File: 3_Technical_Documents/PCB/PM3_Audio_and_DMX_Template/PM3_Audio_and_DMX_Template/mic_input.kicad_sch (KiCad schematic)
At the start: 14 parts, among them U4 OPA322

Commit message: new push
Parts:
- renumbered C6 to C14, C7 to C15, C8 to C16, C9 to C17, C10 to C18, R11 to R15, R12 to R16, R13 to R17, R14 to R18, R15 to R19, R16 to R20, TP14 to TP10, U4 to U6
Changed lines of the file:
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@@
 		(dnp no)
 		(fields_autoplaced yes)
-		(property "Reference" "C8"
+		(property "Reference" "C16"
 			(at 99.06 39.37 90)
 			(effects
@@
 			(project ""
 				(path "/1f276d59-ad9b-4e70-a842-f3b7e562eb9b/2329d9ea-d5d7-4913-84c5-e85a54af032e/0553e14e-9a48-4ba5-90f9-f0331f773f30"
-					(reference "C8")
+					(reference "C16")
 					(unit 1)
 				)
@@
 		(dnp no)
 		(fields_autoplaced yes)
-		(property "Reference" "#PWR034"
+		(property "Reference" "#PWR048"
 			(at 53.34 115.57 0)
 			(effects
@@
 			(project ""
 				(path "/1f276d59-ad9b-4e70-a842-f3b7e562eb9b/2329d9ea-d5d7-4913-84c5-e85a54af032e/0553e14e-9a48-4ba5-90f9-f0331f773f30"
-					(reference "#PWR034")
+					(reference "#PWR048")
 					(unit 1)
 				)
@@
 		(dnp no)
 		(fields_autoplaced yes)
-		(property "Reference" "#PWR040"
+		(property "Reference" "#PWR054"
 			(at 153.67 111.76 0)
 			(effects
@@
 			(project ""
 				(path "/1f276d59-ad9b-4e70-a842-f3b7e562eb9b/2329d9ea-d5d7-4913-84c5-e85a54af032e/0553e14e-9a48-4ba5-90f9-f0331f773f30"
-					(reference "#PWR040")
+					(reference "#PWR054")
 					(unit 1)
 				)
@@
 		(dnp no)
 		(fields_autoplaced yes)
-		(property "Reference" "C7"
+		(property "Reference" "C15"
 			(at 78.359 77.47 90)
 			(effects
@@
 			(project ""
 				(path "/1f276d59-ad9b-4e70-a842-f3b7e562eb9b/2329d9ea-d5d7-4913-84c5-e85a54af032e/0553e14e-9a48-4ba5-90f9-f0331f773f30"
-					(reference "C7")
+					(reference "C15")
 					(unit 1)
 				)
@@
 		(dnp no)
 		(fields_autoplaced yes)
-		(property "Reference" "R13"
+		(property "Reference" "R17"
 			(at 86.36 113.0299 0)
 			(effects
@@
 			(project ""
 				(path "/1f276d59-ad9b-4e70-a842-f3b7e562eb9b/2329d9ea-d5d7-4913-84c5-e85a54af032e/0553e14e-9a48-4ba5-90f9-f0331f773f30"
-					(reference "R13")
+					(reference "R17")
 					(unit 1)
 				)
@@
 		(dnp no)
 		(fields_autoplaced yes)
-		(property "Reference" "R12"
+		(property "Reference" "R16"
 			(at 86.36 100.3299 0)
 			(effects
@@
 			(project ""
 				(path "/1f276d59-ad9b-4e70-a842-f3b7e562eb9b/2329d9ea-d5d7-4913-84c5-e85a54af032e/0553e14e-9a48-4ba5-90f9-f0331f773f30"
-					(reference "R12")
+					(reference "R16")
 					(unit 1)
 				)
@@
 		(dnp no)
 		(fields_autoplaced yes)
-		(property "Reference" "#PWR037"
+		(property "Reference" "#PWR051"
 			(at 99.06 128.27 0)
 			(effects
@@
 			(project "PM3_Audio_and_DMX"
 				(path "/1f276d59-ad9b-4e70-a842-f3b7e562eb9b/2329d9ea-d5d7-4913-84c5-e85a54af032e/0553e14e-9a48-4ba5-90f9-f0331f773f30"
-					(reference "#PWR037")
+					(reference "#PWR051")
 					(unit 1)
 				)
@@
 		(dnp no)
 		(fields_autoplaced yes)
-		(property "Reference" "C9"
+		(property "Reference" "C17"
 			(at 102.87 113.0299 0)
 			(effects
@@
 			(project "PM3_Audio_and_DMX"
 				(path "/1f276d59-ad9b-4e70-a842-f3b7e562eb9b/2329d9ea-d5d7-4913-84c5-e85a54af032e/0553e14e-9a48-4ba5-90f9-f0331f773f30"
-					(reference "C9")
+					(reference "C17")
 					(unit 1)
 				)
@@
 		(dnp no)
 		(fields_autoplaced yes)
-		(property "Reference" "R14"
+		(property "Reference" "R18"
 			(at 99.06 55.88 90)
 			(effects
@@
 			(project ""
 				(path "/1f276d59-ad9b-4e70-a842-f3b7e562eb9b/2329d9ea-d5d7-4913-84c5-e85a54af032e/0553e14e-9a48-4ba5-90f9-f0331f773f30"
-					(reference "R14")
+					(reference "R18")
 					(unit 1)
 				)
@@
 		(dnp no)
 		(fields_autoplaced yes)
-		(property "Reference" "R16"
+		(property "Reference" "R20"
 			(at 156.21 95.2499 0)
 			(effects
@@
 			(project ""
 				(path "/1f276d59-ad9b-4e70-a842-f3b7e562eb9b/2329d9ea-d5d7-4913-84c5-e85a54af032e/0553e14e-9a48-4ba5-90f9-f0331f773f30"
-					(reference "R16")
+					(reference "R20")
 					(unit 1)
 				)
@@
 		(dnp no)
 		(fields_autoplaced yes)
-		(property "Reference" "C6"
+		(property "Reference" "C14"
 			(at 76.2 113.0299 0)
 			(effects
@@
 			(project ""
 				(path "/1f276d59-ad9b-4e70-a842-f3b7e562eb9b/2329d9ea-d5d7-4913-84c5-e85a54af032e/0553e14e-9a48-4ba5-90f9-f0331f773f30"
-					(reference "C6")
+					(reference "C14")
 					(unit 1)
 				)
@@
 		(dnp no)
 		(fields_autoplaced yes)
-		(property "Reference" "#PWR033"
+		(property "Reference" "#PWR047"
 			(at 53.34 64.77 0)
 			(effects
@@
 			(project ""
 				(path "/1f276d59-ad9b-4e70-a842-f3b7e562eb9b/2329d9ea-d5d7-4913-84c5-e85a54af032e/0553e14e-9a48-4ba5-90f9-f0331f773f30"
-					(reference "#PWR033")
+					(reference "#PWR047")
 					(unit 1)
 				)
@@
 		(dnp no)
 		(fields_autoplaced yes)
-		(property "Reference" "R11"
+		(property "Reference" "R15"
 			(at 55.88 72.3899 0)
 			(effects
@@
 			(project ""
 				(path "/1f276d59-ad9b-4e70-a842-f3b7e562eb9b/2329d9ea-d5d7-4913-84c5-e85a54af032e/0553e14e-9a48-4ba5-90f9-f0331f773f30"
-					(reference "R11")
+					(reference "R15")
 					(unit 1)
 				)
@@
 		(dnp no)
 		(fields_autoplaced yes)
-		(property "Reference" "R15"
+		(property "Reference" "R19"
 			(at 128.27 81.28 90)
 			(effects
@@
 			(project ""
 				(path "/1f276d59-ad9b-4e70-a842-f3b7e562eb9b/2329d9ea-d5d7-4913-84c5-e85a54af032e/0553e14e-9a48-4ba5-90f9-f0331f773f30"
-					(reference "R15")
+					(reference "R19")
 					(unit 1)
 				)
@@
 		(on_board yes)
 		(dnp no)
-		(property "Reference" "U4"
+		(property "Reference" "U6"
 			(at 103.632 92.964 0)
 			(effects
@@
 			(project ""
 				(path "/1f276d59-ad9b-4e70-a842-f3b7e562eb9b/2329d9ea-d5d7-4913-84c5-e85a54af032e/0553e14e-9a48-4ba5-90f9-f0331f773f30"
-					(reference "U4")
+					(reference "U6")
 					(unit 1)
 				)
@@
 		(dnp no)
 		(fields_autoplaced yes)
-		(property "Reference" "#PWR038"
+		(property "Reference" "#PWR052"
 			(at 105.41 106.68 0)
 			(effects
@@
 			(project ""
 				(path "/1f276d59-ad9b-4e70-a842-f3b7e562eb9b/2329d9ea-d5d7-4913-84c5-e85a54af032e/0553e14e-9a48-4ba5-90f9-f0331f773f30"
-					(reference "#PWR038")
+					(reference "#PWR052")
 					(unit 1)
 				)
@@
 		(dnp no)
 		(fields_autoplaced yes)
-		(property "Reference" "#PWR039"
+		(property "Reference" "#PWR053"
 			(at 113.03 81.28 0)
 			(effects
@@
 			(project ""
 				(path "/1f276d59-ad9b-4e70-a842-f3b7e562eb9b/2329d9ea-d5d7-4913-84c5-e85a54af032e/0553e14e-9a48-4ba5-90f9-f0331f773f30"
-					(reference "#PWR039")
+					(reference "#PWR053")
 					(unit 1)
 				)
@@
 		(dnp no)
 		(fields_autoplaced yes)
-		(property "Reference" "#PWR035"
+		(property "Reference" "#PWR049"
 			(at 83.82 97.79 0)
 			(effects
@@
 			(project ""
 				(path "/1f276d59-ad9b-4e70-a842-f3b7e562eb9b/2329d9ea-d5d7-4913-84c5-e85a54af032e/0553e14e-9a48-4ba5-90f9-f0331f773f30"
-					(reference "#PWR035")
+					(reference "#PWR049")
 					(unit 1)
 				)
@@
 		(dnp no)
 		(fields_autoplaced yes)
-		(property "Reference" "TP14"
+		(property "Reference" "TP10"
 			(at 41.91 76.7079 0)
 			(effects
@@
 			(project "PM3_Audio_and_DMX"
 				(path "/1f276d59-ad9b-4e70-a842-f3b7e562eb9b/2329d9ea-d5d7-4913-84c5-e85a54af032e/0553e14e-9a48-4ba5-90f9-f0331f773f30"
-					(reference "TP14")
+					(reference "TP10")
 					(unit 1)
 				)
@@
 		(dnp no)
 		(fields_autoplaced yes)
-		(property "Reference" "C10"
+		(property "Reference" "C18"
 			(at 141.351 80.01 90)
 			(effects
@@
 			(project ""
 				(path "/1f276d59-ad9b-4e70-a842-f3b7e562eb9b/2329d9ea-d5d7-4913-84c5-e85a54af032e/0553e14e-9a48-4ba5-90f9-f0331f773f30"
-					(reference "C10")
+					(reference "C18")
 					(unit 1)
 				)
@@
 		(dnp no)
 		(fields_autoplaced yes)
-		(property "Reference" "#PWR036"
+		(property "Reference" "#PWR050"
 			(at 83.82 129.54 0)
 			(effects
@@
 			(project ""
 				(path "/1f276d59-ad9b-4e70-a842-f3b7e562eb9b/2329d9ea-d5d7-4913-84c5-e85a54af032e/0553e14e-9a48-4ba5-90f9-f0331f773f30"
-					(reference "#PWR036")
-					(unit 1)
-				)
+					(reference "#PWR050")
+					(unit 1)
+				)

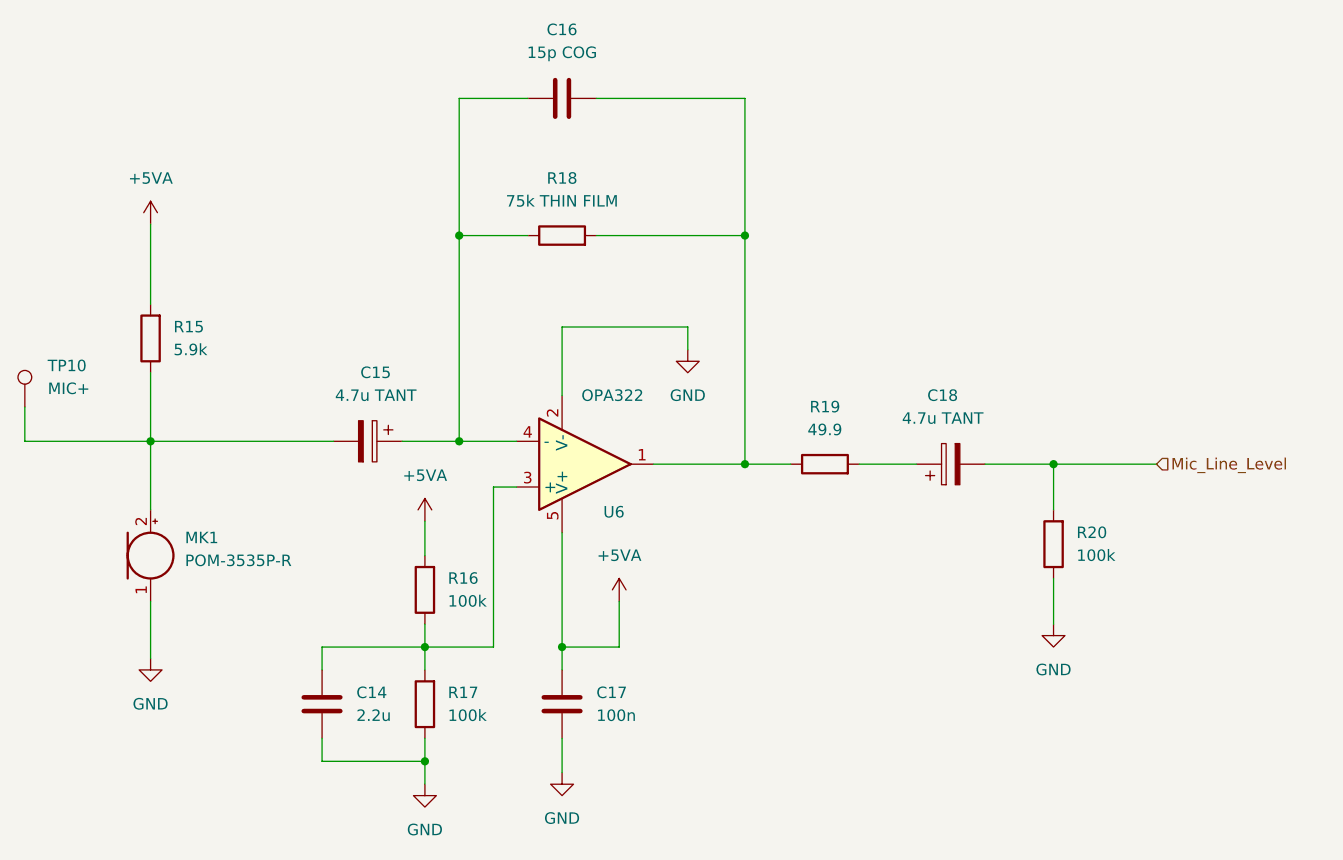
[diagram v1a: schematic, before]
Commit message: rework esp32, codec and layout
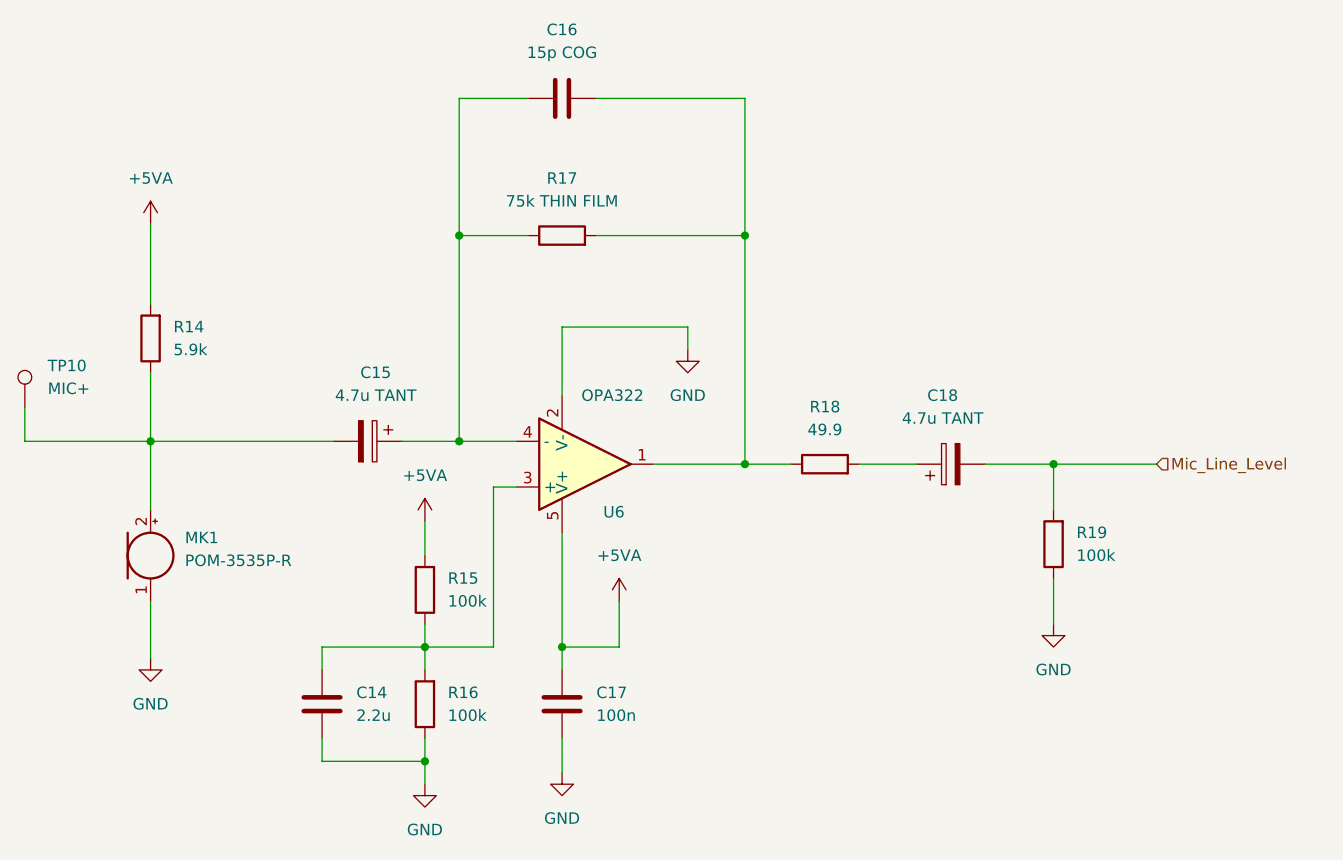
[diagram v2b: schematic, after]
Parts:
- renumbered R15 to R14, R16 to R15, R17 to R16, R18 to R17, R19 to R18, R20 to R19
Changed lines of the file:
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@@
 		(dnp no)
 		(fields_autoplaced yes)
-		(property "Reference" "#PWR048"
+		(property "Reference" "#PWR047"
 			(at 53.34 115.57 0)
 			(effects
@@
 			(project ""
 				(path "/1f276d59-ad9b-4e70-a842-f3b7e562eb9b/2329d9ea-d5d7-4913-84c5-e85a54af032e/0553e14e-9a48-4ba5-90f9-f0331f773f30"
-					(reference "#PWR048")
+					(reference "#PWR047")
 					(unit 1)
 				)
@@
 		(dnp no)
 		(fields_autoplaced yes)
-		(property "Reference" "#PWR054"
+		(property "Reference" "#PWR053"
 			(at 153.67 111.76 0)
 			(effects
@@
 			(project ""
 				(path "/1f276d59-ad9b-4e70-a842-f3b7e562eb9b/2329d9ea-d5d7-4913-84c5-e85a54af032e/0553e14e-9a48-4ba5-90f9-f0331f773f30"
-					(reference "#PWR054")
+					(reference "#PWR053")
 					(unit 1)
 				)
@@
 		(dnp no)
 		(fields_autoplaced yes)
-		(property "Reference" "R17"
+		(property "Reference" "R16"
 			(at 86.36 113.0299 0)
 			(effects
@@
 			(project ""
 				(path "/1f276d59-ad9b-4e70-a842-f3b7e562eb9b/2329d9ea-d5d7-4913-84c5-e85a54af032e/0553e14e-9a48-4ba5-90f9-f0331f773f30"
-					(reference "R17")
+					(reference "R16")
 					(unit 1)
 				)
@@
 		(dnp no)
 		(fields_autoplaced yes)
-		(property "Reference" "R16"
+		(property "Reference" "R15"
 			(at 86.36 100.3299 0)
 			(effects
@@
 			(project ""
 				(path "/1f276d59-ad9b-4e70-a842-f3b7e562eb9b/2329d9ea-d5d7-4913-84c5-e85a54af032e/0553e14e-9a48-4ba5-90f9-f0331f773f30"
-					(reference "R16")
+					(reference "R15")
 					(unit 1)
 				)
@@
 		(dnp no)
 		(fields_autoplaced yes)
-		(property "Reference" "#PWR051"
+		(property "Reference" "#PWR050"
 			(at 99.06 128.27 0)
 			(effects
@@
 			(project "PM3_Audio_and_DMX"
 				(path "/1f276d59-ad9b-4e70-a842-f3b7e562eb9b/2329d9ea-d5d7-4913-84c5-e85a54af032e/0553e14e-9a48-4ba5-90f9-f0331f773f30"
-					(reference "#PWR051")
+					(reference "#PWR050")
 					(unit 1)
 				)
@@
 		(dnp no)
 		(fields_autoplaced yes)
-		(property "Reference" "R18"
+		(property "Reference" "R17"
 			(at 99.06 55.88 90)
 			(effects
@@
 			(project ""
 				(path "/1f276d59-ad9b-4e70-a842-f3b7e562eb9b/2329d9ea-d5d7-4913-84c5-e85a54af032e/0553e14e-9a48-4ba5-90f9-f0331f773f30"
-					(reference "R18")
+					(reference "R17")
 					(unit 1)
 				)
@@
 		(dnp no)
 		(fields_autoplaced yes)
-		(property "Reference" "R20"
+		(property "Reference" "R19"
 			(at 156.21 95.2499 0)
 			(effects
@@
 			(project ""
 				(path "/1f276d59-ad9b-4e70-a842-f3b7e562eb9b/2329d9ea-d5d7-4913-84c5-e85a54af032e/0553e14e-9a48-4ba5-90f9-f0331f773f30"
-					(reference "R20")
+					(reference "R19")
 					(unit 1)
 				)
@@
 		(dnp no)
 		(fields_autoplaced yes)
-		(property "Reference" "#PWR047"
+		(property "Reference" "#PWR046"
 			(at 53.34 64.77 0)
 			(effects
@@
 			(project ""
 				(path "/1f276d59-ad9b-4e70-a842-f3b7e562eb9b/2329d9ea-d5d7-4913-84c5-e85a54af032e/0553e14e-9a48-4ba5-90f9-f0331f773f30"
-					(reference "#PWR047")
+					(reference "#PWR046")
 					(unit 1)
 				)
@@
 		(dnp no)
 		(fields_autoplaced yes)
-		(property "Reference" "R15"
+		(property "Reference" "R14"
 			(at 55.88 72.3899 0)
 			(effects
@@
 			(project ""
 				(path "/1f276d59-ad9b-4e70-a842-f3b7e562eb9b/2329d9ea-d5d7-4913-84c5-e85a54af032e/0553e14e-9a48-4ba5-90f9-f0331f773f30"
-					(reference "R15")
+					(reference "R14")
 					(unit 1)
 				)
@@
 		(dnp no)
 		(fields_autoplaced yes)
-		(property "Reference" "R19"
+		(property "Reference" "R18"
 			(at 128.27 81.28 90)
 			(effects
@@
 			(project ""
 				(path "/1f276d59-ad9b-4e70-a842-f3b7e562eb9b/2329d9ea-d5d7-4913-84c5-e85a54af032e/0553e14e-9a48-4ba5-90f9-f0331f773f30"
-					(reference "R19")
+					(reference "R18")
 					(unit 1)
 				)
@@
 		(dnp no)
 		(fields_autoplaced yes)
-		(property "Reference" "#PWR052"
+		(property "Reference" "#PWR051"
 			(at 105.41 106.68 0)
 			(effects
@@
 			(project ""
 				(path "/1f276d59-ad9b-4e70-a842-f3b7e562eb9b/2329d9ea-d5d7-4913-84c5-e85a54af032e/0553e14e-9a48-4ba5-90f9-f0331f773f30"
-					(reference "#PWR052")
+					(reference "#PWR051")
 					(unit 1)
 				)
@@
 		(dnp no)
 		(fields_autoplaced yes)
-		(property "Reference" "#PWR053"
+		(property "Reference" "#PWR052"
 			(at 113.03 81.28 0)
 			(effects
@@
 			(project ""
 				(path "/1f276d59-ad9b-4e70-a842-f3b7e562eb9b/2329d9ea-d5d7-4913-84c5-e85a54af032e/0553e14e-9a48-4ba5-90f9-f0331f773f30"
-					(reference "#PWR053")
+					(reference "#PWR052")
 					(unit 1)
 				)
@@
 		(dnp no)
 		(fields_autoplaced yes)
-		(property "Reference" "#PWR049"
+		(property "Reference" "#PWR048"
 			(at 83.82 97.79 0)
 			(effects
@@
 			(project ""
 				(path "/1f276d59-ad9b-4e70-a842-f3b7e562eb9b/2329d9ea-d5d7-4913-84c5-e85a54af032e/0553e14e-9a48-4ba5-90f9-f0331f773f30"
-					(reference "#PWR049")
+					(reference "#PWR048")
 					(unit 1)
 				)
@@
 		(dnp no)
 		(fields_autoplaced yes)
-		(property "Reference" "#PWR050"
+		(property "Reference" "#PWR049"
 			(at 83.82 129.54 0)
 			(effects
@@
 			(project ""
 				(path "/1f276d59-ad9b-4e70-a842-f3b7e562eb9b/2329d9ea-d5d7-4913-84c5-e85a54af032e/0553e14e-9a48-4ba5-90f9-f0331f773f30"
-					(reference "#PWR050")
-					(unit 1)
-				)
+					(reference "#PWR049")
+					(unit 1)
+				)

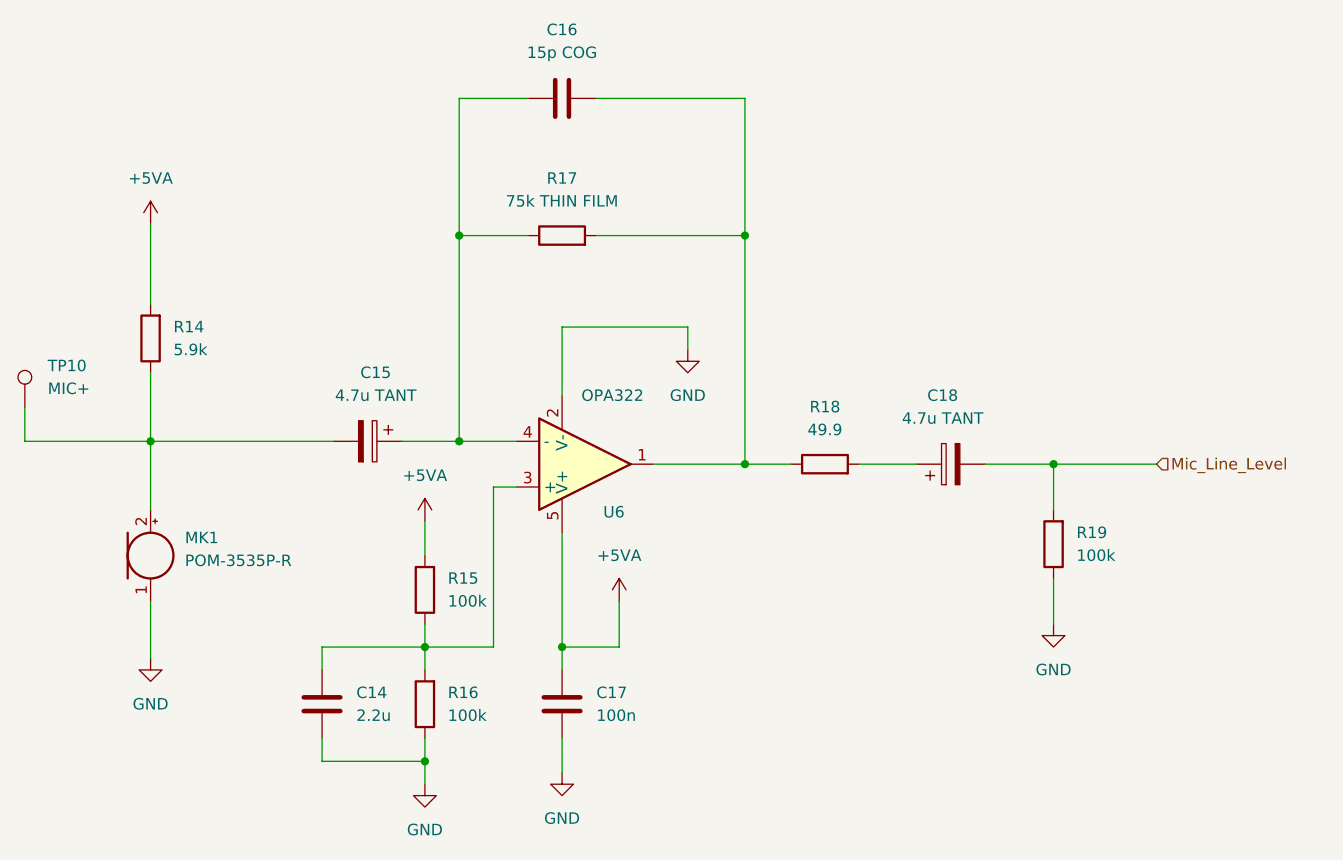
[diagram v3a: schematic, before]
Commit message: schematics, layout and bom updated (to match corrections)
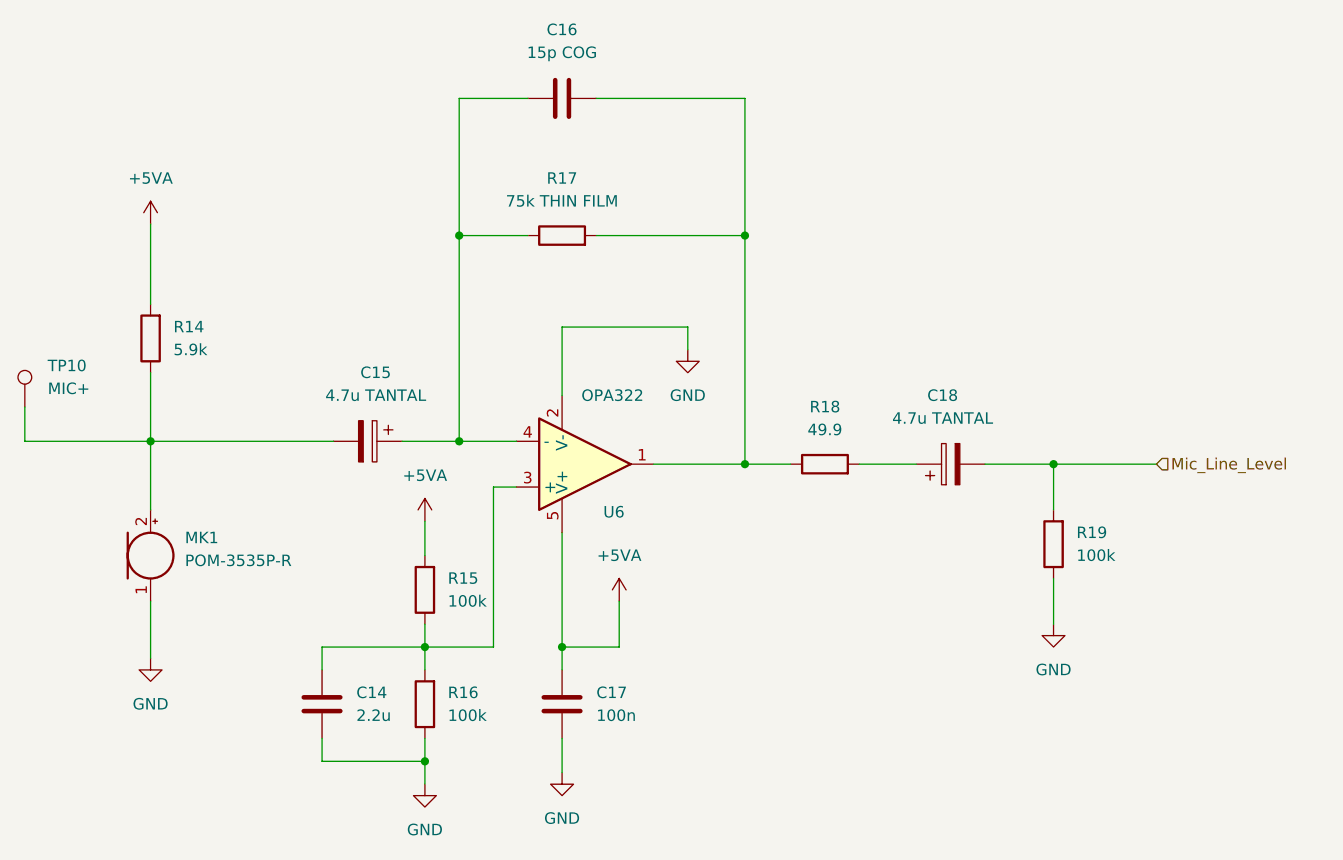
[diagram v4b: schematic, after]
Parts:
- C15, C18: value 4.7u TANT -> 4.7u TANTAL
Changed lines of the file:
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@@
 			)
 		)
-		(property "Value" "4.7u TANT"
+		(property "Value" "4.7u TANTAL"
 			(at 78.359 80.01 90)
 			(effects
@@
 			)
 		)
-		(property "Value" "4.7u TANT"
+		(property "Value" "4.7u TANTAL"
 			(at 141.351 82.55 90)
 			(effects
